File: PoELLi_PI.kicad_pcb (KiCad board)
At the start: 2 copper layers, 85 x 56 mm, 46 parts, among them J1 RJSSE-5080, J2 RJSSE-5380, P1 CONN_02X20, P101 CONN_01X01, P102 CONN_01X01, P2 CONN_01X02, U1 AG9800

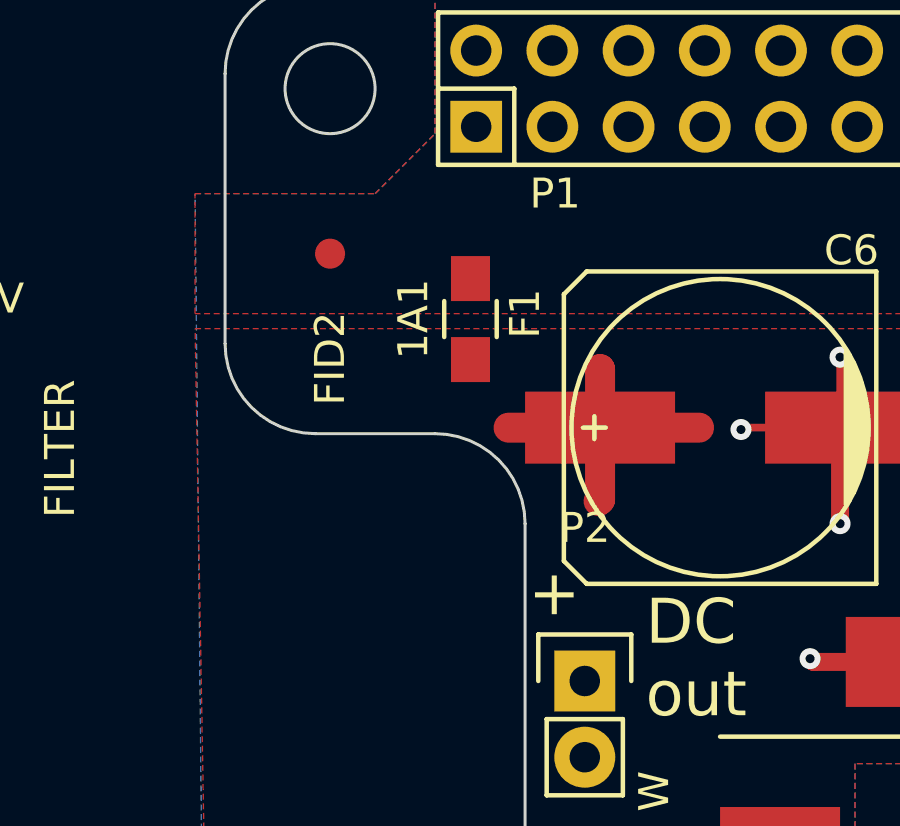
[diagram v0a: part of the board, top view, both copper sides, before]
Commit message: Add protection diodes, output connector, footprints for adjustment resistors
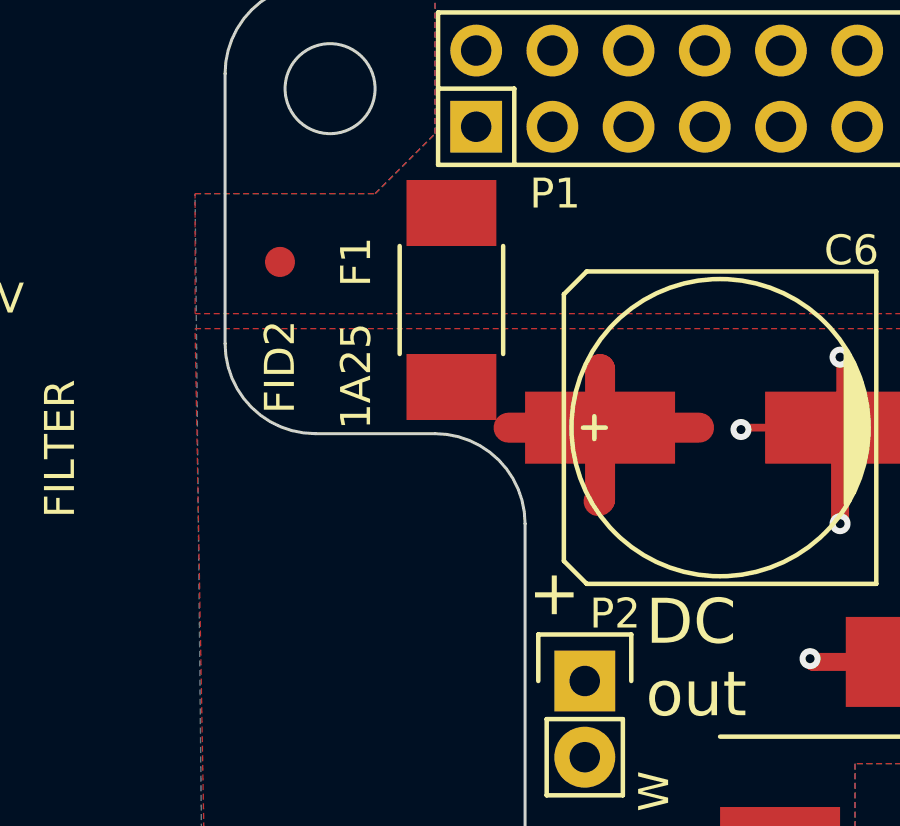
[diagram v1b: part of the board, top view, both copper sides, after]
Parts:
- F1: footprint Resistors_SMD:R_0805_HandSoldering -> Capacitors_SMD:C_1812_HandSoldering
- moved FID2 1.69 mm to (36.8, 41.3)
- moved F1 0.90 mm to (42.5, 42.5)
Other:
- board text added: "1A25"
- board text removed: "1A1"
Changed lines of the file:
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@@
     (links 84)
     (no_connects 0)
-    (area 34.949999 31.949999 120.050001 88.050001)
+    (area 5.383143 -8.824 146.950191 114.424)
     (thickness 1.6)
     (drawings 119)
@@
   )
   (module project_specific:Fiducial_2mm_dia (layer F.Cu)
-    (at 38.5 41)
+    (at 36.83 41.275)
     (fp_text reference FID2 (at 0 3.5 90) (layer F.SilkS)
       (effects (font (size 1 1) (thickness 0.15)))
@@
     (pad 9 smd rect (at 5.715 -0.8 90) (size 6.25 3.2) (layers F.Cu F.Paste F.Mask)
       (net 10 GNDA))
-  )
-  (module Resistors_SMD:R_0805_HandSoldering (layer F.Cu)
-    (at 43.18 43.18 90)
-    (descr "Resistor SMD 0805, hand soldering")
-    (tags "resistor 0805")
-    (attr smd)
-    (fp_text reference F1 (at 0.18 1.82 90) (layer F.SilkS)
-      (effects (font (size 1 1) (thickness 0.15)))
-    )
-    (fp_text value FUSE (at 0 2.1 90) (layer F.Fab)
-      (effects (font (size 1 1) (thickness 0.15)))
-    )
-    (fp_line (start -2.4 -1) (end 2.4 -1) (layer F.CrtYd) (width 0.05))
-    (fp_line (start -2.4 1) (end 2.4 1) (layer F.CrtYd) (width 0.05))
-    (fp_line (start -2.4 -1) (end -2.4 1) (layer F.CrtYd) (width 0.05))
-    (fp_line (start 2.4 -1) (end 2.4 1) (layer F.CrtYd) (width 0.05))
-    (fp_line (start 0.6 0.875) (end -0.6 0.875) (layer F.SilkS) (width 0.15))
-    (fp_line (start -0.6 -0.875) (end 0.6 -0.875) (layer F.SilkS) (width 0.15))
-    (pad 1 smd rect (at -1.35 0 90) (size 1.5 1.3) (layers F.Cu F.Paste F.Mask)
-      (net 63 /AG_OUT_+))
-    (pad 2 smd rect (at 1.35 0 90) (size 1.5 1.3) (layers F.Cu F.Paste F.Mask)
-      (net 13 +5V))
-    (model Resistors_SMD.3dshapes/R_0805_HandSoldering.wrl
-      (at (xyz 0 0 0))
-      (scale (xyz 1 1 1))
-      (rotate (xyz 0 0 0))
-    )
   )
   (module Diodes_SMD:SOD-323 (layer F.Cu)
@@
     (descr "Through hole pin header")
     (tags "pin header")
-    (fp_text reference P2 (at 0 -5.1) (layer F.SilkS)
+    (fp_text reference P2 (at 1.01 -2.245) (layer F.SilkS)
       (effects (font (size 1 1) (thickness 0.15)))
     )
@@
     )
   )
+  (module Capacitors_SMD:C_1812_HandSoldering (layer F.Cu)
+    (at 42.545 42.545 90)
+    (descr "Capacitor SMD 1812, hand soldering")
+    (tags "capacitor 1812")
+    (attr smd)
+    (fp_text reference F1 (at 1.27 -3.175 90) (layer F.SilkS)
+      (effects (font (size 1 1) (thickness 0.15)))
+    )
+    (fp_text value FUSE (at 0 3 90) (layer F.Fab)
+      (effects (font (size 1 1) (thickness 0.15)))
+    )
+    (fp_line (start -4.3 -1.85) (end 4.3 -1.85) (layer F.CrtYd) (width 0.05))
+    (fp_line (start -4.3 1.85) (end 4.3 1.85) (layer F.CrtYd) (width 0.05))
+    (fp_line (start -4.3 -1.85) (end -4.3 1.85) (layer F.CrtYd) (width 0.05))
+    (fp_line (start 4.3 -1.85) (end 4.3 1.85) (layer F.CrtYd) (width 0.05))
+    (fp_line (start 1.8 -1.725) (end -1.8 -1.725) (layer F.SilkS) (width 0.15))
+    (fp_line (start -1.8 1.725) (end 1.8 1.725) (layer F.SilkS) (width 0.15))
+    (pad 1 smd rect (at -2.9 0 90) (size 2.2 3) (layers F.Cu F.Paste F.Mask)
+      (net 63 /AG_OUT_+))
+    (pad 2 smd rect (at 2.9 0 90) (size 2.2 3) (layers F.Cu F.Paste F.Mask)
+      (net 13 +5V))
+    (model Capacitors_SMD.3dshapes/C_1812_HandSoldering.wrl
+      (at (xyz 0 0 0))
+      (scale (xyz 1 1 1))
+      (rotate (xyz 0 0 0))
+    )
+  )
   (gr_text Down (at 46.101 79.629 90) (layer F.SilkS)
     (effects (font (size 1.5 1.5) (thickness 0.3)))
@@
   (gr_line (start 112.75 59.5) (end 120 59.5) (angle 90) (layer Margin) (width 2))
   (gr_line (start 121.623 65.619) (end 99.623 65.619) (angle 90) (layer Margin) (width 2))
-  (gr_text 1A1 (at 41.275 43.18 90) (layer F.SilkS)
+  (gr_text 1A25 (at 39.37 45.085 90) (layer F.SilkS)
     (effects (font (size 1 1) (thickness 0.2)))
   )

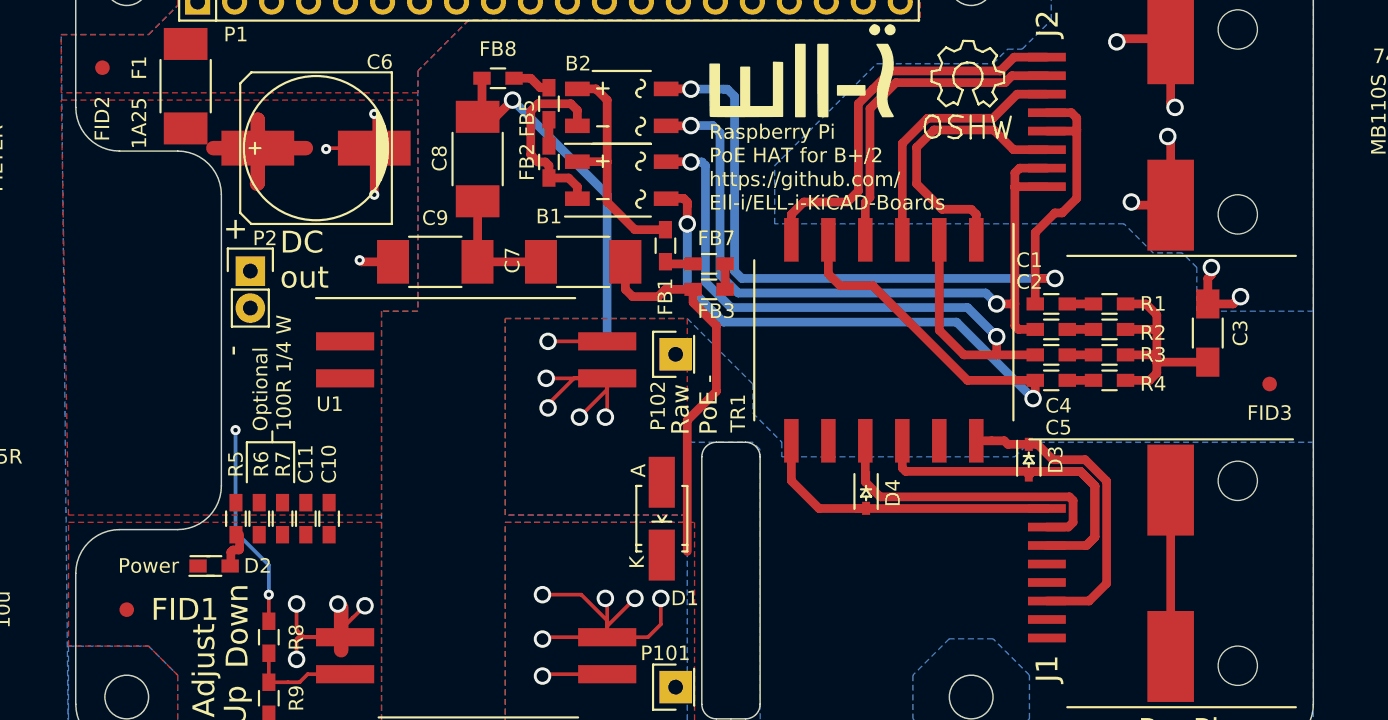
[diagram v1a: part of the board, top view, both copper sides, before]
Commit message: Fix name on silkscreen, change fuse
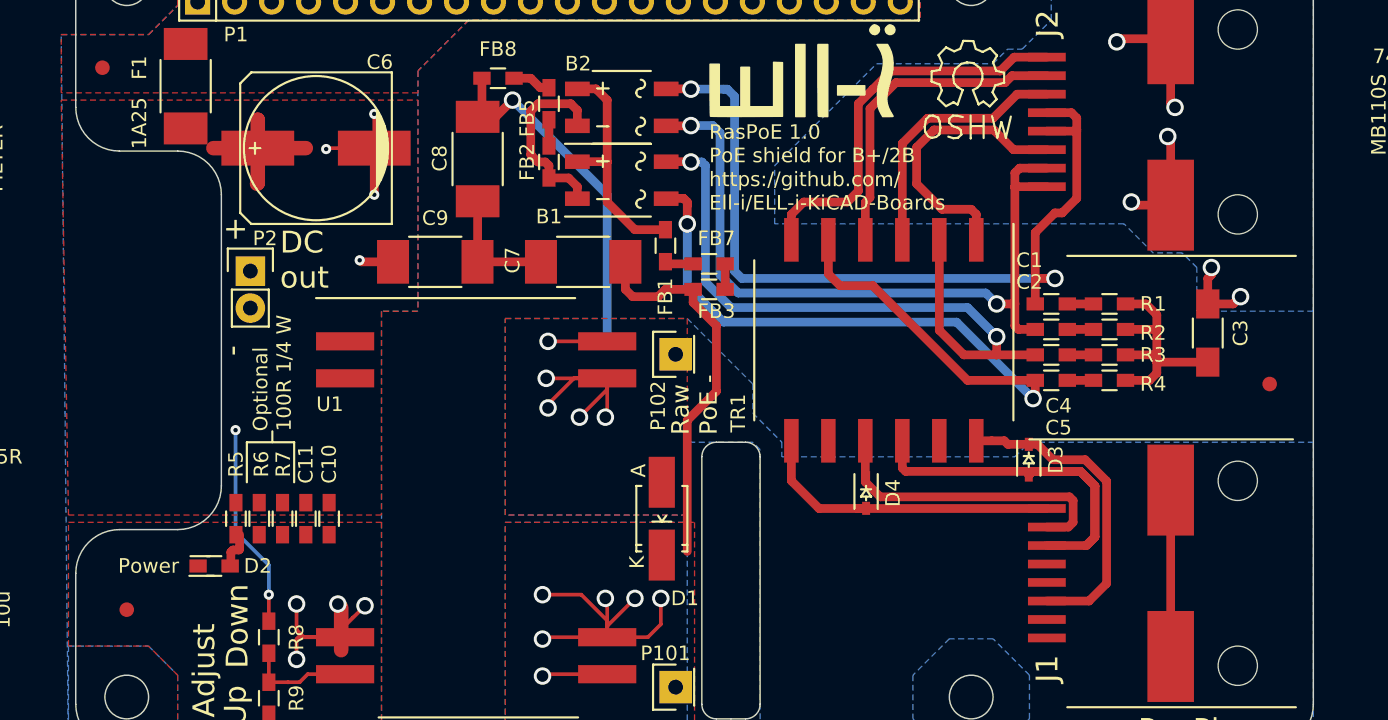
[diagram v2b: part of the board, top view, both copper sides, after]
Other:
- board text added: "RasPoE 1.0 PoE shield for B+/2B"
- board text removed: "Raspberry Pi PoE HAT for B+/2"
